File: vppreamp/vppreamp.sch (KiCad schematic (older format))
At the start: 24 parts, among them J1 Input, J2 Output, SW1 On, U1 TL072

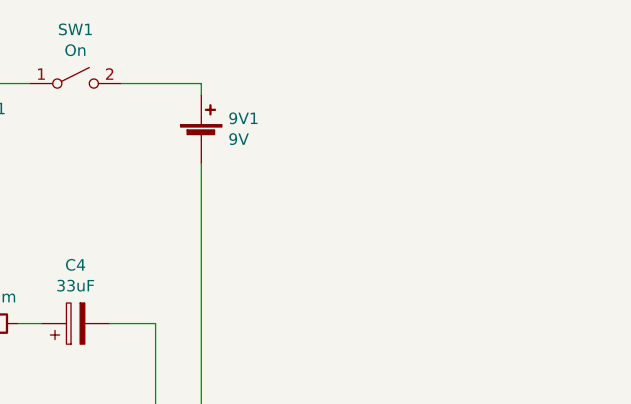
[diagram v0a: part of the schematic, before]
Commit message: added power jack
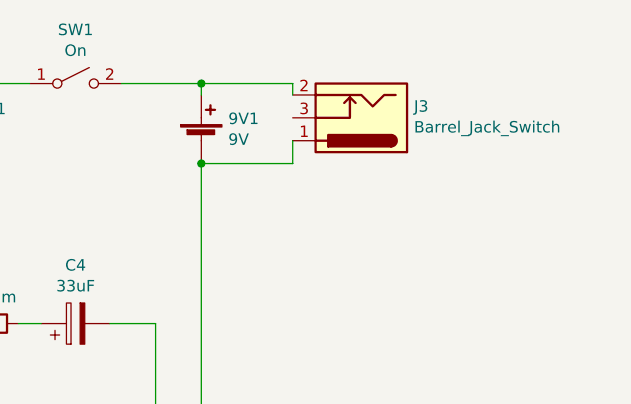
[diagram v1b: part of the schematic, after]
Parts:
- added J3: Barrel_Jack_Switch, Connector_BarrelJack:BarrelJack_Horizontal, symbol Connector:Barrel_Jack_Switch
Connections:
- net GND: now also J3.1
- net at 9V1.1 (+), SW1.2 (B): now also J3.2
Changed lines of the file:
@@
 	1    0    0    -1
 $EndComp
+$Comp
+L Connector:Barrel_Jack_Switch J3
+U 1 1 5FBE8FDA
+P 8650 2500
+F 0 "J3" H 8420 2450 50  0000 R CNN
+F 1 "Barrel_Jack_Switch" H 8420 2541 50  0000 R CNN
+F 2 "Connector_BarrelJack:BarrelJack_Horizontal" H 8700 2460 50  0001 C CNN
+F 3 "~" H 8700 2460 50  0001 C CNN
+	1    8650 2500
+	-1   0    0    1
+$EndComp
+Wire Wire Line
+	7950 2700 8350 2700
+Wire Wire Line
+	8350 2700 8350 2600
+Connection ~ 7950 2700
+Wire Wire Line
+	7950 2350 8350 2350
+Wire Wire Line
+	8350 2350 8350 2400
+Connection ~ 7950 2350
 $EndSCHEMATC

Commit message: add jacks, remap for v2
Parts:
- added InJack1: InJack, NateLibrary:StereoJackTRS3, symbol Connector_Generic:Conn_01x06
- added OutJack1: OutJack, NateLibrary:StereoJackTRS3, symbol Connector_Generic:Conn_01x06
- C2, Cf1, Cin1: footprint Capacitor_THT:C_Axial_L5.1mm_D3.1mm_P7.50mm_Horizontal -> Capacitor_THT:C_Disc_D7.5mm_W2.5mm_P5.00mm
- R1, R2, R3, R4, R5, R6, R7, Rf1: footprint Resistor_THT:R_Axial_DIN0309_L9.0mm_D3.2mm_P12.70mm_Horizontal -> Resistor_THT:R_Axial_DIN0207_L6.3mm_D2.5mm_P7.62mm_Horizontal
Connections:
- wire segments 73 -> 82
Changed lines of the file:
@@
 EESchema Schematic File Version 4
-EELAYER 30 0
+LIBS:vppreamp-cache
+EELAYER 26 0
 EELAYER END
 $Descr A4 11693 8268
@@
 F 0 "R1" H 2820 2546 50  0000 L CNN
 F 1 "10k" H 2820 2455 50  0000 L CNN
-F 2 "Resistor_THT:R_Axial_DIN0309_L9.0mm_D3.2mm_P12.70mm_Horizontal" V 2680 2500 50  0001 C CNN
+F 2 "Resistor_THT:R_Axial_DIN0207_L6.3mm_D2.5mm_P7.62mm_Horizontal" V 2680 2500 50  0001 C CNN
 F 3 "~" H 2750 2500 50  0001 C CNN
 	1    2750 2500
@@
 F 0 "R2" H 2820 3846 50  0000 L CNN
 F 1 "10k" H 2820 3755 50  0000 L CNN
-F 2 "Resistor_THT:R_Axial_DIN0309_L9.0mm_D3.2mm_P12.70mm_Horizontal" V 2680 3800 50  0001 C CNN
+F 2 "Resistor_THT:R_Axial_DIN0207_L6.3mm_D2.5mm_P7.62mm_Horizontal" V 2680 3800 50  0001 C CNN
 F 3 "~" H 2750 3800 50  0001 C CNN
 	1    2750 3800
 	1    0    0    -1
 $EndComp
-Wire Wire Line
-	2500 3300 2500 4250
 Wire Wire Line
 	2500 4250 2750 4250
@@
 F 0 "Cin1" V 2948 3200 50  0000 C CNN
 F 1 "100n" V 3039 3200 50  0000 C CNN
-F 2 "Capacitor_THT:C_Axial_L5.1mm_D3.1mm_P7.50mm_Horizontal" H 3238 3050 50  0001 C CNN
+F 2 "Capacitor_THT:C_Disc_D7.5mm_W2.5mm_P5.00mm" H 3238 3050 50  0001 C CNN
 F 3 "~" H 3200 3200 50  0001 C CNN
 	1    3200 3200
@@
 $EndComp
 Wire Wire Line
-	2500 3200 3050 3200
+	2500 3200 2600 3200
 Wire Wire Line
 	2750 2650 2750 2850
@@
 F 0 "Rf1" V 4443 3700 50  0000 C CNN
 F 1 "1M" V 4534 3700 50  0000 C CNN
-F 2 "Resistor_THT:R_Axial_DIN0309_L9.0mm_D3.2mm_P12.70mm_Horizontal" V 4580 3700 50  0001 C CNN
+F 2 "Resistor_THT:R_Axial_DIN0207_L6.3mm_D2.5mm_P7.62mm_Horizontal" V 4580 3700 50  0001 C CNN
 F 3 "~" H 4650 3700 50  0001 C CNN
 	1    4650 3700
@@
 F 0 "Cf1" V 4348 4100 50  0000 C CNN
 F 1 "10n" V 4439 4100 50  0000 C CNN
-F 2 "Capacitor_THT:C_Axial_L5.1mm_D3.1mm_P7.50mm_Horizontal" H 4638 3950 50  0001 C CNN
+F 2 "Capacitor_THT:C_Disc_D7.5mm_W2.5mm_P5.00mm" H 4638 3950 50  0001 C CNN
 F 3 "~" H 4600 4100 50  0001 C CNN
 	1    4600 4100
@@
 F 0 "C2" V 4998 3100 50  0000 C CNN
 F 1 "220n" V 5089 3100 50  0000 C CNN
-F 2 "Capacitor_THT:C_Axial_L5.1mm_D3.1mm_P7.50mm_Horizontal" H 5288 2950 50  0001 C CNN
+F 2 "Capacitor_THT:C_Disc_D7.5mm_W2.5mm_P5.00mm" H 5288 2950 50  0001 C CNN
 F 3 "~" H 5250 3100 50  0001 C CNN
 	1    5250 3100
@@
 F 0 "R7" H 6870 2846 50  0000 L CNN
 F 1 "10k" H 6870 2755 50  0000 L CNN
-F 2 "Resistor_THT:R_Axial_DIN0309_L9.0mm_D3.2mm_P12.70mm_Horizontal" V 6730 2800 50  0001 C CNN
+F 2 "Resistor_THT:R_Axial_DIN0207_L6.3mm_D2.5mm_P7.62mm_Horizontal" V 6730 2800 50  0001 C CNN
 F 3 "~" H 6800 2800 50  0001 C CNN
 	1    6800 2800
@@
 F 0 "R3" H 5720 2846 50  0000 L CNN
 F 1 "22k" H 5720 2755 50  0000 L CNN
-F 2 "Resistor_THT:R_Axial_DIN0309_L9.0mm_D3.2mm_P12.70mm_Horizontal" V 5580 2800 50  0001 C CNN
+F 2 "Resistor_THT:R_Axial_DIN0207_L6.3mm_D2.5mm_P7.62mm_Horizontal" V 5580 2800 50  0001 C CNN
 F 3 "~" H 5650 2800 50  0001 C CNN
 	1    5650 2800
@@
 F 0 "R4" V 5893 3900 50  0000 C CNN
 F 1 "10k" V 5984 3900 50  0000 C CNN
-F 2 "Resistor_THT:R_Axial_DIN0309_L9.0mm_D3.2mm_P12.70mm_Horizontal" V 6030 3900 50  0001 C CNN
+F 2 "Resistor_THT:R_Axial_DIN0207_L6.3mm_D2.5mm_P7.62mm_Horizontal" V 6030 3900 50  0001 C CNN
 F 3 "~" H 6100 3900 50  0001 C CNN
 	1    6100 3900
@@
 F 0 "R5" H 5780 4154 50  0000 R CNN
 F 1 "10k" H 5780 4245 50  0000 R CNN
-F 2 "Resistor_THT:R_Axial_DIN0309_L9.0mm_D3.2mm_P12.70mm_Horizontal" V 5780 4200 50  0001 C CNN
+F 2 "Resistor_THT:R_Axial_DIN0207_L6.3mm_D2.5mm_P7.62mm_Horizontal" V 5780 4200 50  0001 C CNN
 F 3 "~" H 5850 4200 50  0001 C CNN
 	1    5850 4200
@@
 F 0 "R6" V 6793 3400 50  0000 C CNN
 F 1 "100ohm" V 6884 3400 50  0000 C CNN
-F 2 "Resistor_THT:R_Axial_DIN0309_L9.0mm_D3.2mm_P12.70mm_Horizontal" V 6930 3400 50  0001 C CNN
+F 2 "Resistor_THT:R_Axial_DIN0207_L6.3mm_D2.5mm_P7.62mm_Horizontal" V 6930 3400 50  0001 C CNN
 F 3 "~" H 7000 3400 50  0001 C CNN
 	1    7000 3400
@@
 F 3 "~" H 8700 2460 50  0001 C CNN
 	1    8650 2500
-	-1   0    0    1
+	-1   0    0    -1
 $EndComp
 Wire Wire Line
@@
 	8350 2350 8350 2400
 Connection ~ 7950 2350
+$Comp
+L Connector_Generic:Conn_01x06 InJack1
+U 1 1 5FBEA7B6
+P 1900 3250
+F 0 "InJack1" H 1820 3667 50  0000 C CNN
+F 1 "InJack" H 1820 3576 50  0000 C CNN
+F 2 "NateLibrary:StereoJackTRS3" H 1900 3250 50  0001 C CNN
+F 3 "~" H 1900 3250 50  0001 C CNN
+	1    1900 3250
+	-1   0    0    1
+$EndComp
+$Comp
+L Connector_Generic:Conn_01x06 OutJack1
+U 1 1 5FBEA893
+P 9200 4150
+F 0 "OutJack1" H 9120 4567 50  0000 C CNN
+F 1 "OutJack" H 9120 4476 50  0000 C CNN
+F 2 "NateLibrary:StereoJackTRS3" H 9200 4150 50  0001 C CNN
+F 3 "~" H 9200 4150 50  0001 C CNN
+	1    9200 4150
+	1    0    0    1
+$EndComp
+Wire Wire Line
+	8350 4050 8350 3950
+Wire Wire Line
+	8350 3950 9000 3950
+Connection ~ 8350 4050
+Wire Wire Line
+	8350 4150 8350 4350
+Wire Wire Line
+	8350 4350 9000 4350
+Connection ~ 8350 4150
+Wire Wire Line
+	2500 3300 2500 3450
+Wire Wire Line
+	2500 3450 2100 3450
+Connection ~ 2500 3450
+Wire Wire Line
+	2500 3450 2500 4250
+Connection ~ 2600 3200
+Wire Wire Line
+	2600 3200 3050 3200
+Wire Wire Line
+	2100 3050 2600 3050
+Wire Wire Line
+	2600 3050 2600 3200
 $EndSCHEMATC
